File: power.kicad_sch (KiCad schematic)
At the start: 19 parts, among them U1 TL072, U2 TL072, U3 TL072, U4 TL072, U5 TL072, U6 TL072, U7 TL072

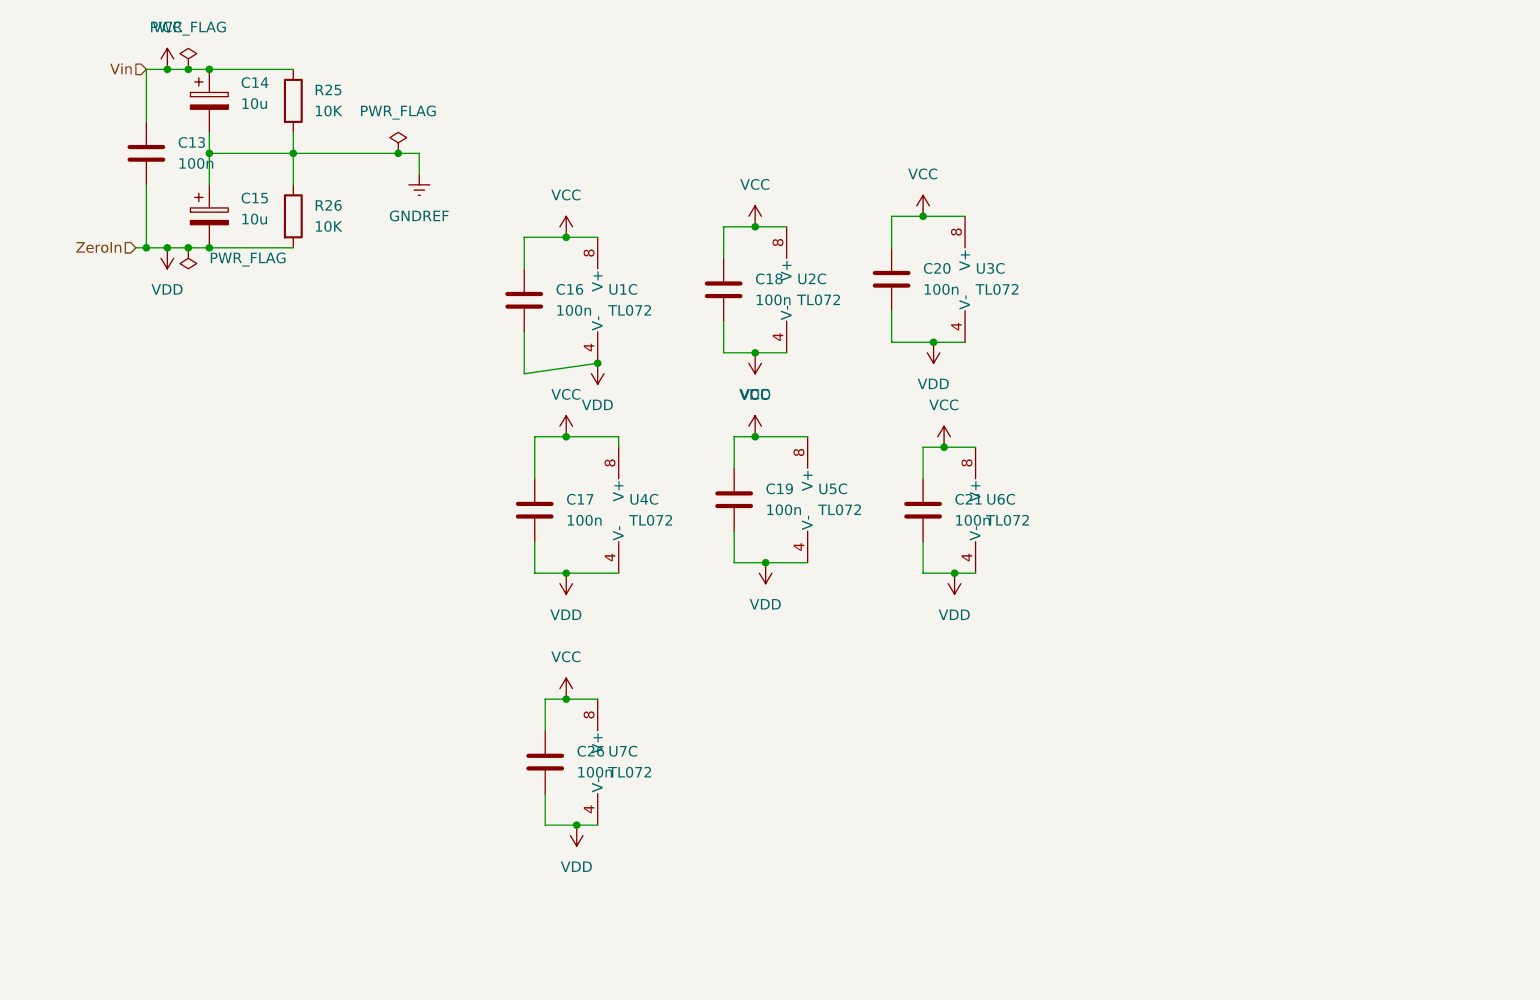
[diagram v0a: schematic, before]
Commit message: Improve power supply decoupling, add LED indicator
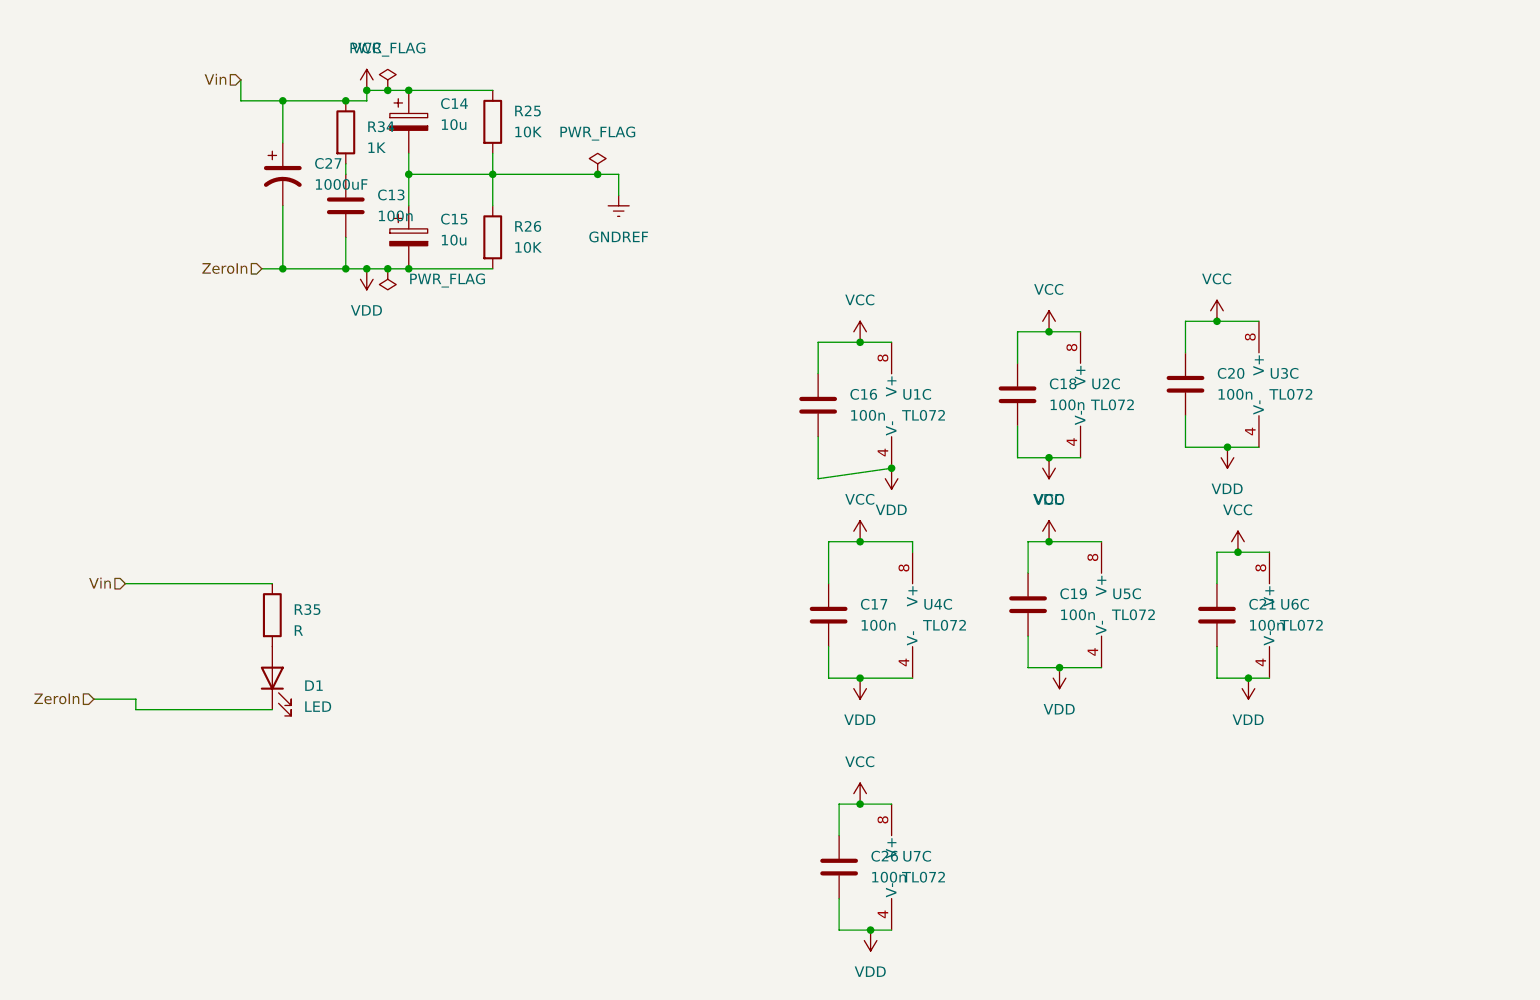
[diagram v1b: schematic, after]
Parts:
- added C27: 1000uF, symbol Device:C_Polarized_US
- added D1: LED, symbol Device:LED
- added R34: 1K, symbol Device:R
- added R35: R, symbol Device:R
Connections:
- net VCC: now also C27.1, R34.1, R35.1; no longer C13.1
- net VDD: now also C27.2, D1.1 (K)
- new net: C13.1, R34.2
- new net: D1.2 (A), R35.2
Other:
- moved on the sheet: C13, C14, C15, C16, C17, C18, C19, C20, C21, C26, R25, R26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

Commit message: Re-annotate and run erc
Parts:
- renumbered C27 to C22, C13 to C23, C14 to C24, C15 to C25, C16 to C26, C17 to C27, C26 to C28, C18 to C29, C19 to C30, C20 to C31, C21 to C32, R35 to R30, R34 to R31, R25 to R32, R26 to R33

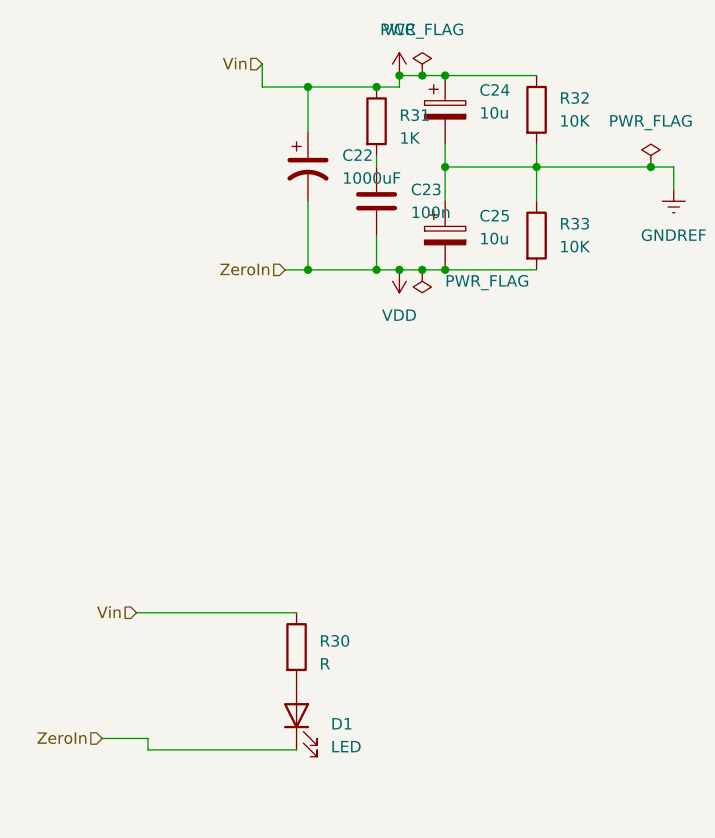
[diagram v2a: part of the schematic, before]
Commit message: Fix some ERC warnings
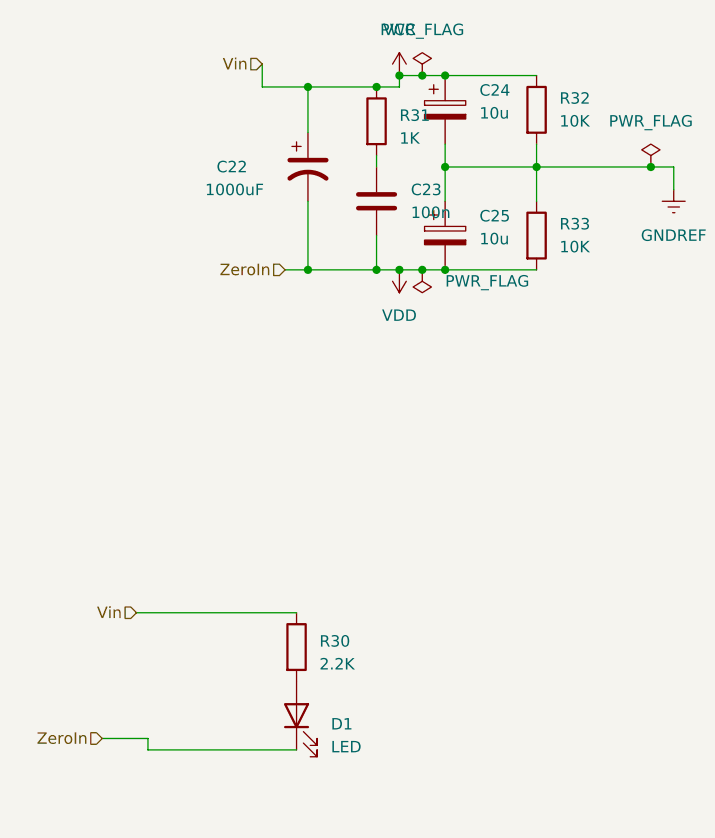
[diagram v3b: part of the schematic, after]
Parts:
- R30: value R -> 2.2K
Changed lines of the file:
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@@
   )
   (symbol (lib_id "Device:C_Polarized_US") (at 44.45 35.56 0) (unit 1)
-    (in_bom yes) (on_board yes) (dnp no) (fields_autoplaced)
-    (property "Reference" "C22" (at 48.26 34.29 0)
-      (effects (font (size 1.27 1.27)) (justify left))
-    )
-    (property "Value" "1000uF" (at 48.26 36.83 0)
+    (in_bom yes) (on_board yes) (dnp no)
+    (property "Reference" "C22" (at 34.29 35.56 0)
+      (effects (font (size 1.27 1.27)) (justify left))
+    )
+    (property "Value" "1000uF" (at 33.02 38.1 0)
       (effects (font (size 1.27 1.27)) (justify left))
     )
@@
       (effects (font (size 1.27 1.27)) (justify left))
     )
-    (property "Value" "R" (at 45.72 90.805 0)
-      (effects (font (size 1.27 1.27)) (justify left))
-    )
+    (property "Value" "2.2K" (at 45.72 90.805 0)
+      (effects (font (size 1.27 1.27)) (justify left))
+    )

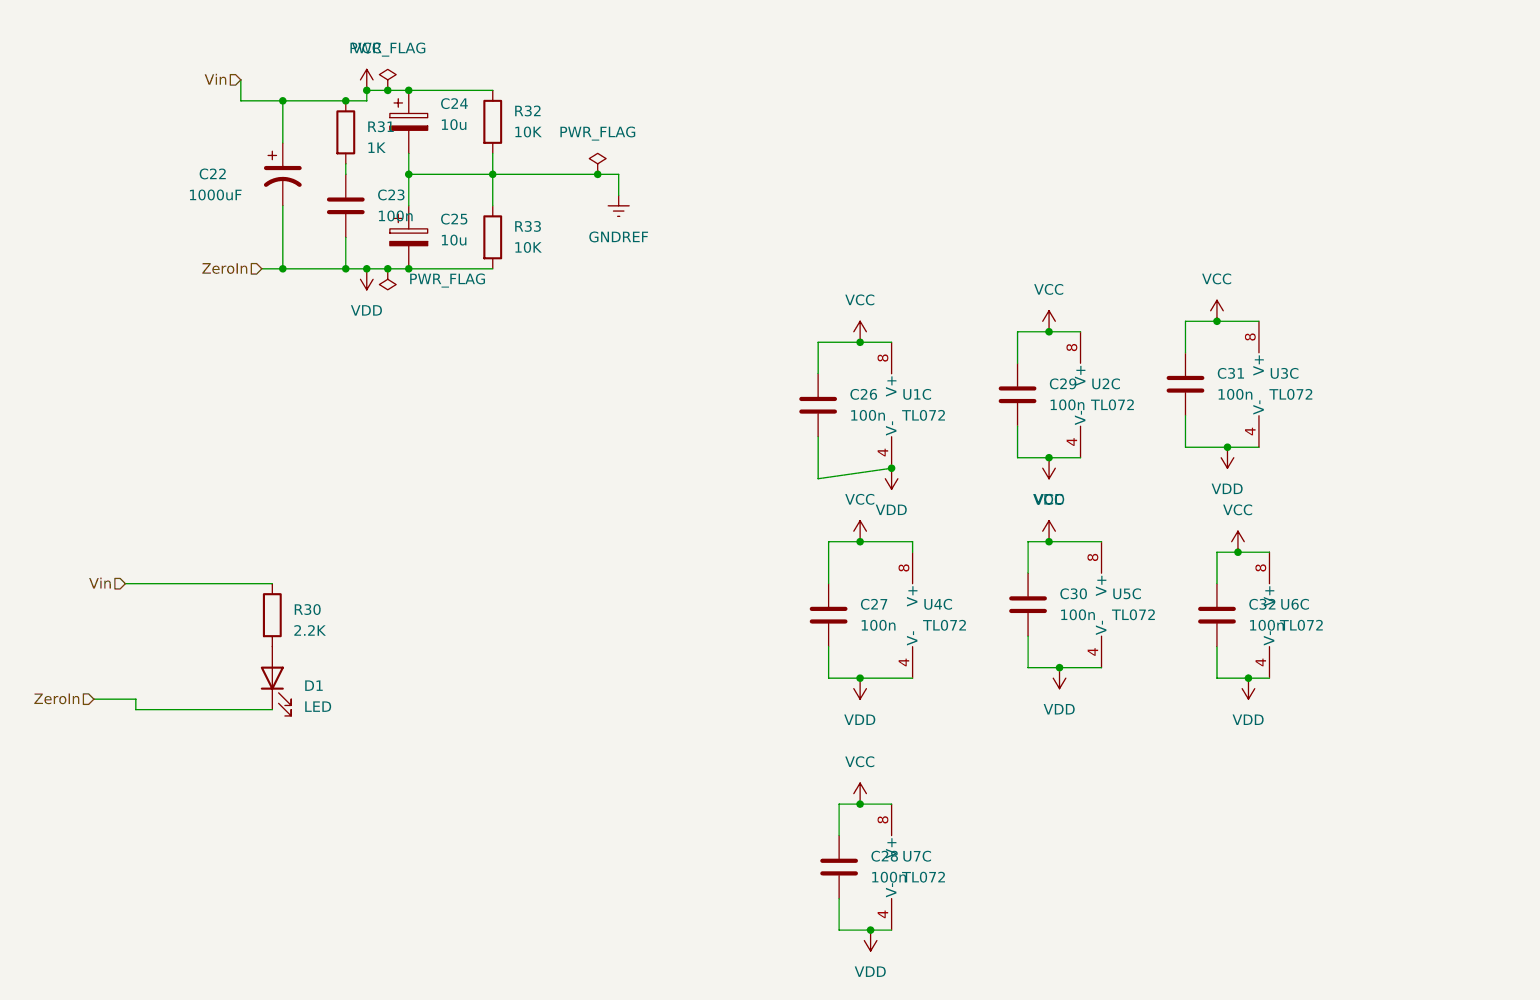
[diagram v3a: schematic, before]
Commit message: Switch to TL074
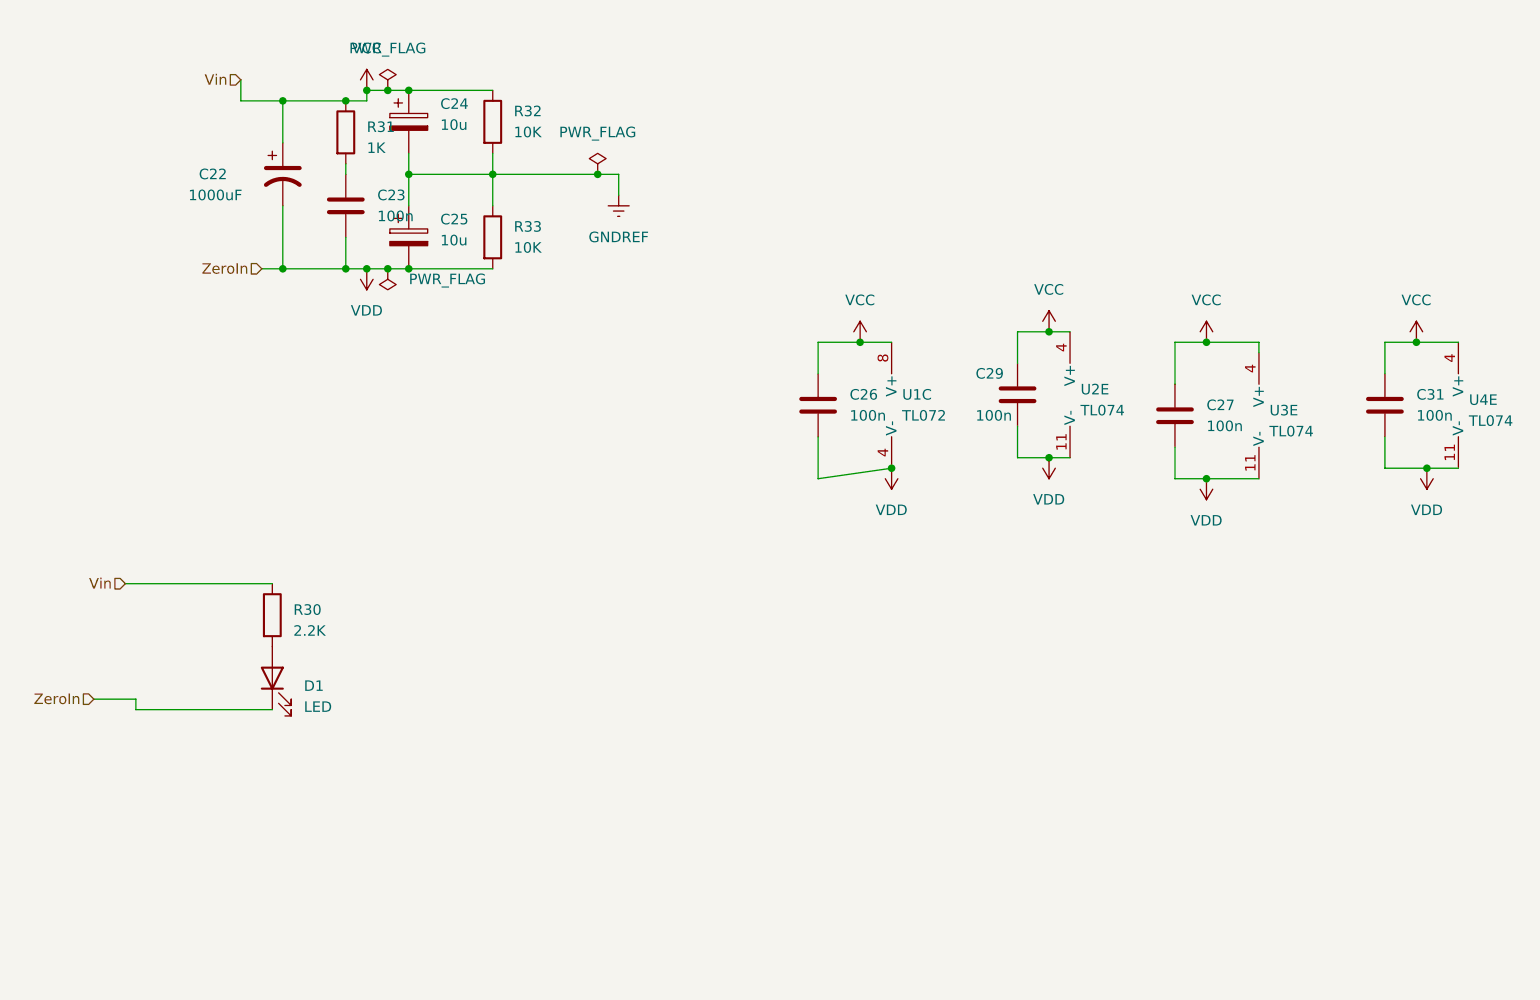
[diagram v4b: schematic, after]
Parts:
- removed C28, C30, C32: 100n, Capacitor_THT:C_Disc_D7.5mm_W5.0mm_P7.50mm, symbol Device:C
- removed U5, U6, U7: TL072, Package_DIP:DIP-8_W7.62mm_Socket, symbol Amplifier_Operational:TL072
- U2: value TL072 -> TL074; footprint Package_DIP:DIP-8_W7.62mm_Socket -> (none); symbol Amplifier_Operational:TL072 -> Amplifier_Operational:TL074
- U3: renamed from U4; value TL072 -> TL074; footprint Package_DIP:DIP-8_W7.62mm_Socket -> (none); symbol Amplifier_Operational:TL072 -> Amplifier_Operational:TL074
- U4: renamed from U3; value TL072 -> TL074; footprint Package_DIP:DIP-8_W7.62mm_Socket -> (none); symbol Amplifier_Operational:TL072 -> Amplifier_Operational:TL074
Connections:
- net VCC: now also U2.4 (V+), U3.4 (V+), U4.4 (V+); no longer U2.8 (V+), U3.8 (V+), U4.8 (V+)
- net VDD: now also U2.11 (V-), U3.11 (V-), U4.11 (V-); no longer U2.4 (V-), U3.4 (V-), U4.4 (V-)
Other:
- moved on the sheet: C27, C31, U2E, U3E, U4E

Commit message: Assign footprints to everything
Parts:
- C22: footprint (none) -> Capacitor_THT:CP_Radial_D10.0mm_P5.00mm
- C23, C26, C27, C29, C31: footprint Capacitor_THT:C_Disc_D7.5mm_W5.0mm_P7.50mm -> Capacitor_SMD:C_0805_2012Metric_Pad1.18x1.45mm_HandSolder
- D1: footprint (none) -> LED_SMD:LED_1210_3225Metric_Pad1.42x2.65mm_HandSolder
- R30: footprint (none) -> Resistor_SMD:R_1210_3225Metric_Pad1.30x2.65mm_HandSolder
- R31: footprint (none) -> Resistor_SMD:R_1206_3216Metric_Pad1.30x1.75mm_HandSolder
- R32, R33: footprint Resistor_THT:R_Axial_DIN0207_L6.3mm_D2.5mm_P7.62mm_Horizontal -> Resistor_SMD:R_1206_3216Metric_Pad1.30x1.75mm_HandSolder
- U2, U3: footprint (none) -> Package_SO:SOIC-14-16_3.9x9.9mm_P1.27mm
- U4: footprint (none) -> Package_SO:SOIC-14_3.9x8.7mm_P1.27mm
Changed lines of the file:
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@@
       (effects (font (size 1.27 1.27)) (justify left))
     )
-    (property "Footprint" "Capacitor_THT:C_Disc_D7.5mm_W5.0mm_P7.50mm" (at 178.7652 67.31 0)
+    (property "Footprint" "Capacitor_SMD:C_0805_2012Metric_Pad1.18x1.45mm_HandSolder" (at 178.7652 67.31 0)
       (effects (font (size 1.27 1.27)) hide)
     )
@@
       (effects (font (size 1.27 1.27)) (justify left))
     )
-    (property "Footprint" "Capacitor_THT:C_Disc_D7.5mm_W5.0mm_P7.50mm" (at 110.1852 67.31 0)
+    (property "Footprint" "Capacitor_SMD:C_0805_2012Metric_Pad1.18x1.45mm_HandSolder" (at 110.1852 67.31 0)
       (effects (font (size 1.27 1.27)) hide)
     )
@@
       (effects (font (size 1.27 1.27)) (justify left))
     )
-    (property "Footprint" "Resistor_THT:R_Axial_DIN0207_L6.3mm_D2.5mm_P7.62mm_Horizontal" (at 68.072 43.18 90)
+    (property "Footprint" "Resistor_SMD:R_1206_3216Metric_Pad1.30x1.75mm_HandSolder" (at 68.072 43.18 90)
       (effects (font (size 1.27 1.27)) hide)
     )
@@
       (effects (font (size 1.27 1.27)) (justify left))
     )
-    (property "Footprint" "Resistor_THT:R_Axial_DIN0207_L6.3mm_D2.5mm_P7.62mm_Horizontal" (at 68.072 29.21 90)
+    (property "Footprint" "Resistor_SMD:R_1206_3216Metric_Pad1.30x1.75mm_HandSolder" (at 68.072 29.21 90)
       (effects (font (size 1.27 1.27)) hide)
     )
@@
       (effects (font (size 1.27 1.27)) (justify left))
     )
-    (property "Footprint" "" (at 163.83 62.23 0)
+    (property "Footprint" "Package_SO:SOIC-14-16_3.9x9.9mm_P1.27mm" (at 163.83 62.23 0)
       (effects (font (size 1.27 1.27)) hide)
     )
@@
       (effects (font (size 1.27 1.27)) (justify left))
     )
-    (property "Footprint" "Capacitor_THT:C_Disc_D7.5mm_W5.0mm_P7.50mm" (at 153.3652 68.58 0)
+    (property "Footprint" "Capacitor_SMD:C_0805_2012Metric_Pad1.18x1.45mm_HandSolder" (at 153.3652 68.58 0)
       (effects (font (size 1.27 1.27)) hide)
     )
@@
       (effects (font (size 1.27 1.27)) (justify left))
     )
-    (property "Footprint" "Capacitor_THT:C_Disc_D7.5mm_W5.0mm_P7.50mm" (at 53.0352 43.18 0)
+    (property "Footprint" "Capacitor_SMD:C_0805_2012Metric_Pad1.18x1.45mm_HandSolder" (at 53.0352 43.18 0)
       (effects (font (size 1.27 1.27)) hide)
     )
@@
       (effects (font (size 1.27 1.27)) (justify left))
     )
-    (property "Footprint" "" (at 50.292 30.48 90)
+    (property "Footprint" "Resistor_SMD:R_1206_3216Metric_Pad1.30x1.75mm_HandSolder" (at 50.292 30.48 90)
       (effects (font (size 1.27 1.27)) hide)
     )
@@
       (effects (font (size 1.27 1.27)) (justify left))
     )
-    (property "Footprint" "" (at 140.97 59.69 0)
+    (property "Footprint" "Package_SO:SOIC-14-16_3.9x9.9mm_P1.27mm" (at 140.97 59.69 0)
       (effects (font (size 1.27 1.27)) hide)
     )
@@
       (effects (font (size 1.27 1.27)) (justify left))
     )
-    (property "Footprint" "Capacitor_THT:C_Disc_D7.5mm_W5.0mm_P7.50mm" (at 134.3152 66.04 0)
+    (property "Footprint" "Capacitor_SMD:C_0805_2012Metric_Pad1.18x1.45mm_HandSolder" (at 134.3152 66.04 0)
       (effects (font (size 1.27 1.27)) hide)
     )
@@
       (effects (font (size 1.27 1.27)) (justify right))
     )
-    (property "Footprint" "" (at 43.18 96.52 0)
+    (property "Footprint" "LED_SMD:LED_1210_3225Metric_Pad1.42x2.65mm_HandSolder" (at 43.18 96.52 0)
       (effects (font (size 1.27 1.27)) hide)
     )
@@
       (effects (font (size 1.27 1.27)) (justify left))
     )
-    (property "Footprint" "" (at 44.45 35.56 0)
+    (property "Footprint" "Capacitor_THT:CP_Radial_D10.0mm_P5.00mm" (at 44.45 35.56 0)
       (effects (font (size 1.27 1.27)) hide)
     )
@@
       (effects (font (size 1.27 1.27)) (justify left))
     )
-    (property "Footprint" "" (at 187.96 60.96 0)
+    (property "Footprint" "Package_SO:SOIC-14_3.9x8.7mm_P1.27mm" (at 187.96 60.96 0)
       (effects (font (size 1.27 1.27)) hide)
     )
@@
       (effects (font (size 1.27 1.27)) (justify left))
     )
-    (property "Footprint" "" (at 41.402 88.9 90)
-      (effects (font (size 1.27 1.27)) hide)
-    )
+    (property "Footprint" "Resistor_SMD:R_1210_3225Metric_Pad1.30x2.65mm_HandSolder" (at 41.402 88.9 90)
+      (effects (font (size 1.27 1.27)) hide)
+    )
